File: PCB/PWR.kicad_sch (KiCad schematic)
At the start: 71 parts, among them Q1 CSD23381F4, U201 STC3115IQT, U203 STPMIC1APQR, U3 BQ24298RTWR

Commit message: PCB_UPDATE
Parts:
- added R222, R223: 0, Resistor_SMD:R_0805_2012Metric, symbol Device:R
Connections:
- net VIN: now also R222.1, R223.2; no longer C233.2, C234.2, L206.2, U3.15 (SYS), U3.16 (SYS)
- net V_USB: now also R222.2
- net CHRG_PSEL renamed CHRG_PSEL_OUT
- new net: C233.2, C234.2, L206.2, R223.1, U3.15 (SYS), U3.16 (SYS)

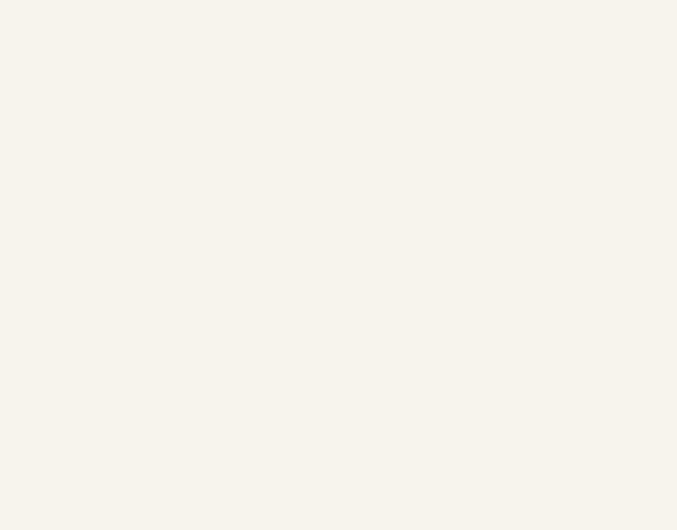
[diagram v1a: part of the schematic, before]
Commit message: bat holder added
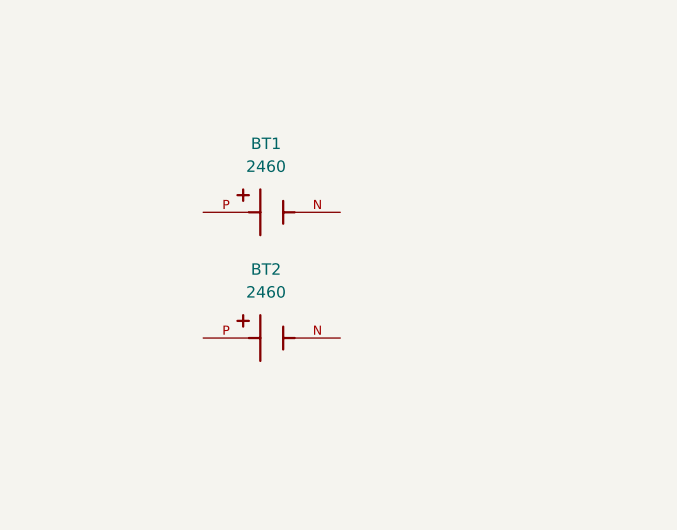
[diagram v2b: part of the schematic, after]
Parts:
- added BT1, BT2: 2460, lib:BAT_2460, symbol 2460:2460
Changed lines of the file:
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@@
+	)
+	(symbol
+		(lib_id "2460:2460")
+		(at 58.42 53.34 0)
+		(unit 1)
+		(exclude_from_sim no)
+		(in_bom yes)
+		(on_board yes)
+		(dnp no)
+		(fields_autoplaced yes)
+		(property "Reference" "BT2"
+			(at 57.785 45.72 0)
+			(effects
+				(font
+					(size 1.27 1.27)
+				)
+			)
+		)
+		(property "Value" "2460"
+			(at 57.785 48.26 0)
+			(effects
+				(font
+					(size 1.27 1.27)
+				)
+			)
+		)
+		(property "Footprint" "lib:BAT_2460"
+			(at 58.42 53.34 0)
+			(effects
+				(font
+					(size 1.27 1.27)
+				)
+				(justify bottom)
+				(hide yes)
+			)
+		)
+		(property "Datasheet" ""
+			(at 58.42 53.34 0)
+			(effects
+				(font
+					(size 1.27 1.27)
+				)
+				(hide yes)
+			)
+		)
+		(property "Description" ""
+			(at 58.42 53.34 0)
+			(effects
+				(font
+					(size 1.27 1.27)
+				)
+				(hide yes)
+			)
+		)
+		(property "PARTREV" "B"
+			(at 58.42 53.34 0)
+			(effects
+				(font
+					(size 1.27 1.27)
+				)
+				(justify bottom)
+				(hide yes)
+			)
+		)
+		(property "STANDARD" "Manufacturer Recommendations"
+			(at 58.42 53.34 0)
+			(effects
+				(font
+					(size 1.27 1.27)
+				)
+				(justify bottom)
+				(hide yes)
+			)
+		)
+		(property "SNAPEDA_PN" "2460"
+			(at 58.42 53.34 0)
+			(effects
+				(font
+					(size 1.27 1.27)
+				)
+				(justify bottom)
+				(hide yes)
+			)
+		)
+		(property "MAXIMUM_PACKAGE_HEIGHT" "14.14mm"
+			(at 58.42 53.34 0)
+			(effects
+				(font
+					(size 1.27 1.27)
+				)
+				(justify bottom)
+				(hide yes)
+			)
+		)
+		(property "MANUFACTURER" "Keystone"
+			(at 58.42 53.34 0)
+			(effects
+				(font
+					(size 1.27 1.27)
+				)
+				(justify bottom)
+				(hide yes)
+			)
+		)
+		(pin "P"
+		)
+		(pin "N"
+		)
+		(instances
+			(project "MPU_MOD"
+				(path "/65890f61-d586-475b-928a-b635a5e4e59e/355c85ef-822d-4607-91cf-41bd60068331"
+					(reference "BT2")
+					(unit 1)
+				)
+			)
+		)
 	)
 	(symbol
@@
 					(unit 1)
 				)
+			)
+		)
+	)
+	(symbol
+		(lib_id "2460:2460")
+		(at 58.42 39.37 0)
+		(unit 1)
+		(exclude_from_sim no)
+		(in_bom yes)
+		(on_board yes)
+		(dnp no)
+		(fields_autoplaced yes)
+		(property "Reference" "BT1"
+			(at 57.785 31.75 0)
+			(effects
+				(font
+					(size 1.27 1.27)
+				)
+			)
+		)
+		(property "Value" "2460"
+			(at 57.785 34.29 0)
+			(effects
+				(font
+					(size 1.27 1.27)
+				)
+			)
+		)
+		(property "Footprint" "lib:BAT_2460"
+			(at 58.42 39.37 0)
+			(effects
+				(font
+					(size 1.27 1.27)
+				)
+				(justify bottom)
+				(hide yes)
+			)
+		)
+		(property "Datasheet" ""
+			(at 58.42 39.37 0)
+			(effects
+				(font
+					(size 1.27 1.27)
+				)
+				(hide yes)
+			)
+		)
+		(property "Description" ""
+			(at 58.42 39.37 0)
+			(effects
+				(font
+					(size 1.27 1.27)
+				)
+				(hide yes)
+			)
+		)
+		(property "PARTREV" "B"
+			(at 58.42 39.37 0)
+			(effects
+				(font
+					(size 1.27 1.27)
+				)
+				(justify bottom)
+				(hide yes)
+			)
+		)
+		(property "STANDARD" "Manufacturer Recommendations"
+			(at 58.42 39.37 0)
+			(effects
+				(font
+					(size 1.27 1.27)
+				)
+				(justify bottom)
+				(hide yes)
+			)
+		)
+		(property "SNAPEDA_PN" "2460"
+			(at 58.42 39.37 0)
+			(effects
+				(font
+					(size 1.27 1.27)
+				)
+				(justify bottom)
+				(hide yes)
+			)
+		)
+		(property "MAXIMUM_PACKAGE_HEIGHT" "14.14mm"
+			(at 58.42 39.37 0)
+			(effects
+				(font
+					(size 1.27 1.27)
+				)
+				(justify bottom)
+				(hide yes)
+			)
+		)
+		(property "MANUFACTURER" "Keystone"
+			(at 58.42 39.37 0)
+			(effects
+				(font
+					(size 1.27 1.27)
+				)
+				(justify bottom)
+				(hide yes)
+			)
+		)
+		(pin "P"
+		)
+		(pin "N"
+		)
+		(instances
+			(project ""
+				(path "/65890f61-d586-475b-928a-b635a5e4e59e/355c85ef-822d-4607-91cf-41bd60068331"
+					(reference "BT1")
+					(unit 1)
+				)
